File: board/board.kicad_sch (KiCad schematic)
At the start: 15 parts, among them J1 020_1000BASE-T_with_CT, J10 018_QSPI, J11 Conn_01x03_Male, J2 003_power, J3 008_USB, J4 001_I2C, J5 008_USB, J6 002_SPI, J7 010_UART, J8 015_RGMII, J9 010_UART, U2 TLV71318PQDBVRQ1

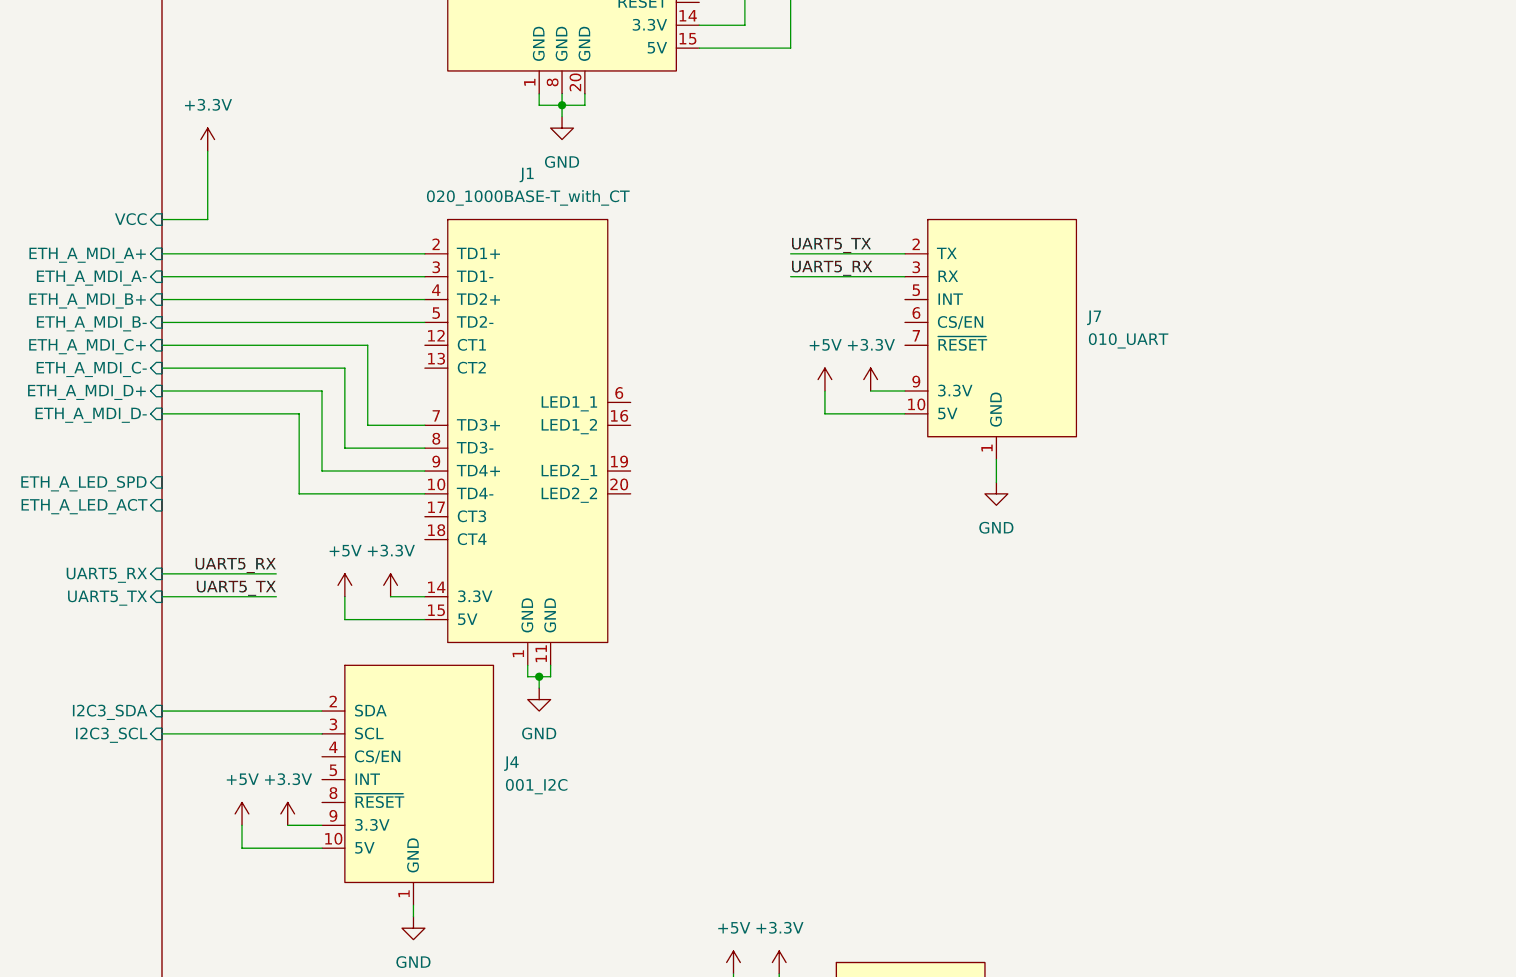
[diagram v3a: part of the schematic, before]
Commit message: increased spacing
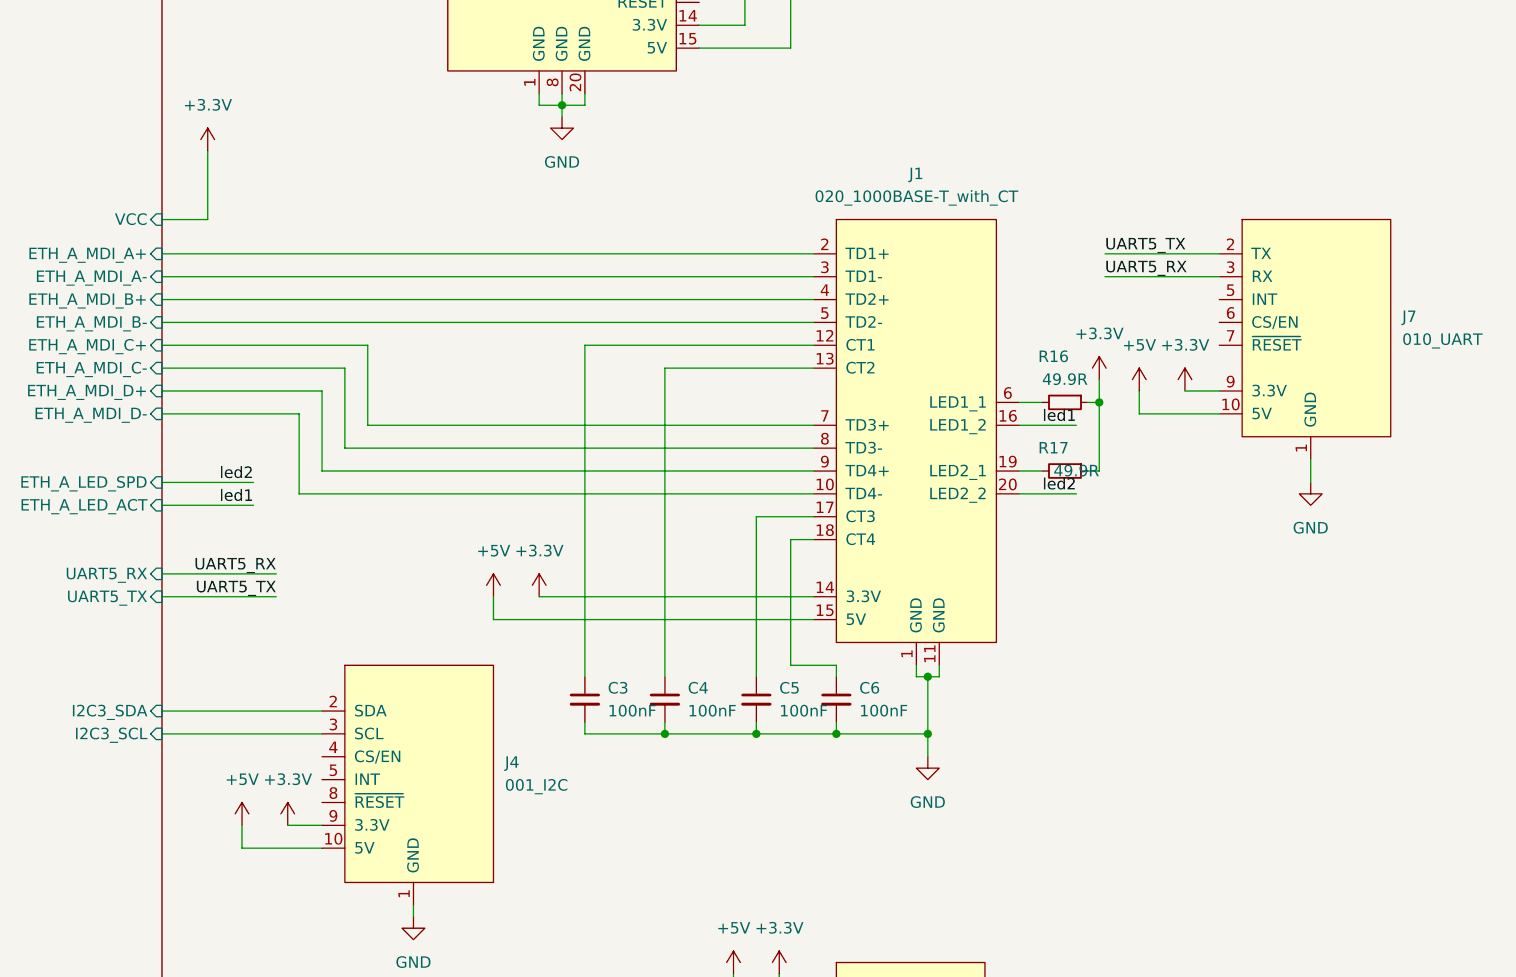
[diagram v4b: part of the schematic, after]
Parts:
- added C3, C4, C5, C6: 100nF, Capacitor_SMD:C_0603_1608Metric, symbol Device:C_Small
- added R16, R17: 49.9R, Resistor_SMD:R_0603_1608Metric, symbol Device:R_Small
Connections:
- net +3.3V: now also R16.1, R17.1
- net GND: now also C3.2, C4.2, C5.2, C6.2
- net at J1.12 (CT1): now also C3.1
- net at J1.13 (CT2): now also C4.1
- net led1: now reaches J1.16 (LED1_2)
- net at J1.17 (CT3): now also C5.1
- net at J1.18 (CT4): now also C6.1
- net at J1.19 (LED2_1): now also R17.2
- net led2: now reaches J1.20 (LED2_2)
- net at J1.6 (LED1_1): now also R16.2
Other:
- moved on the sheet: J1, J7

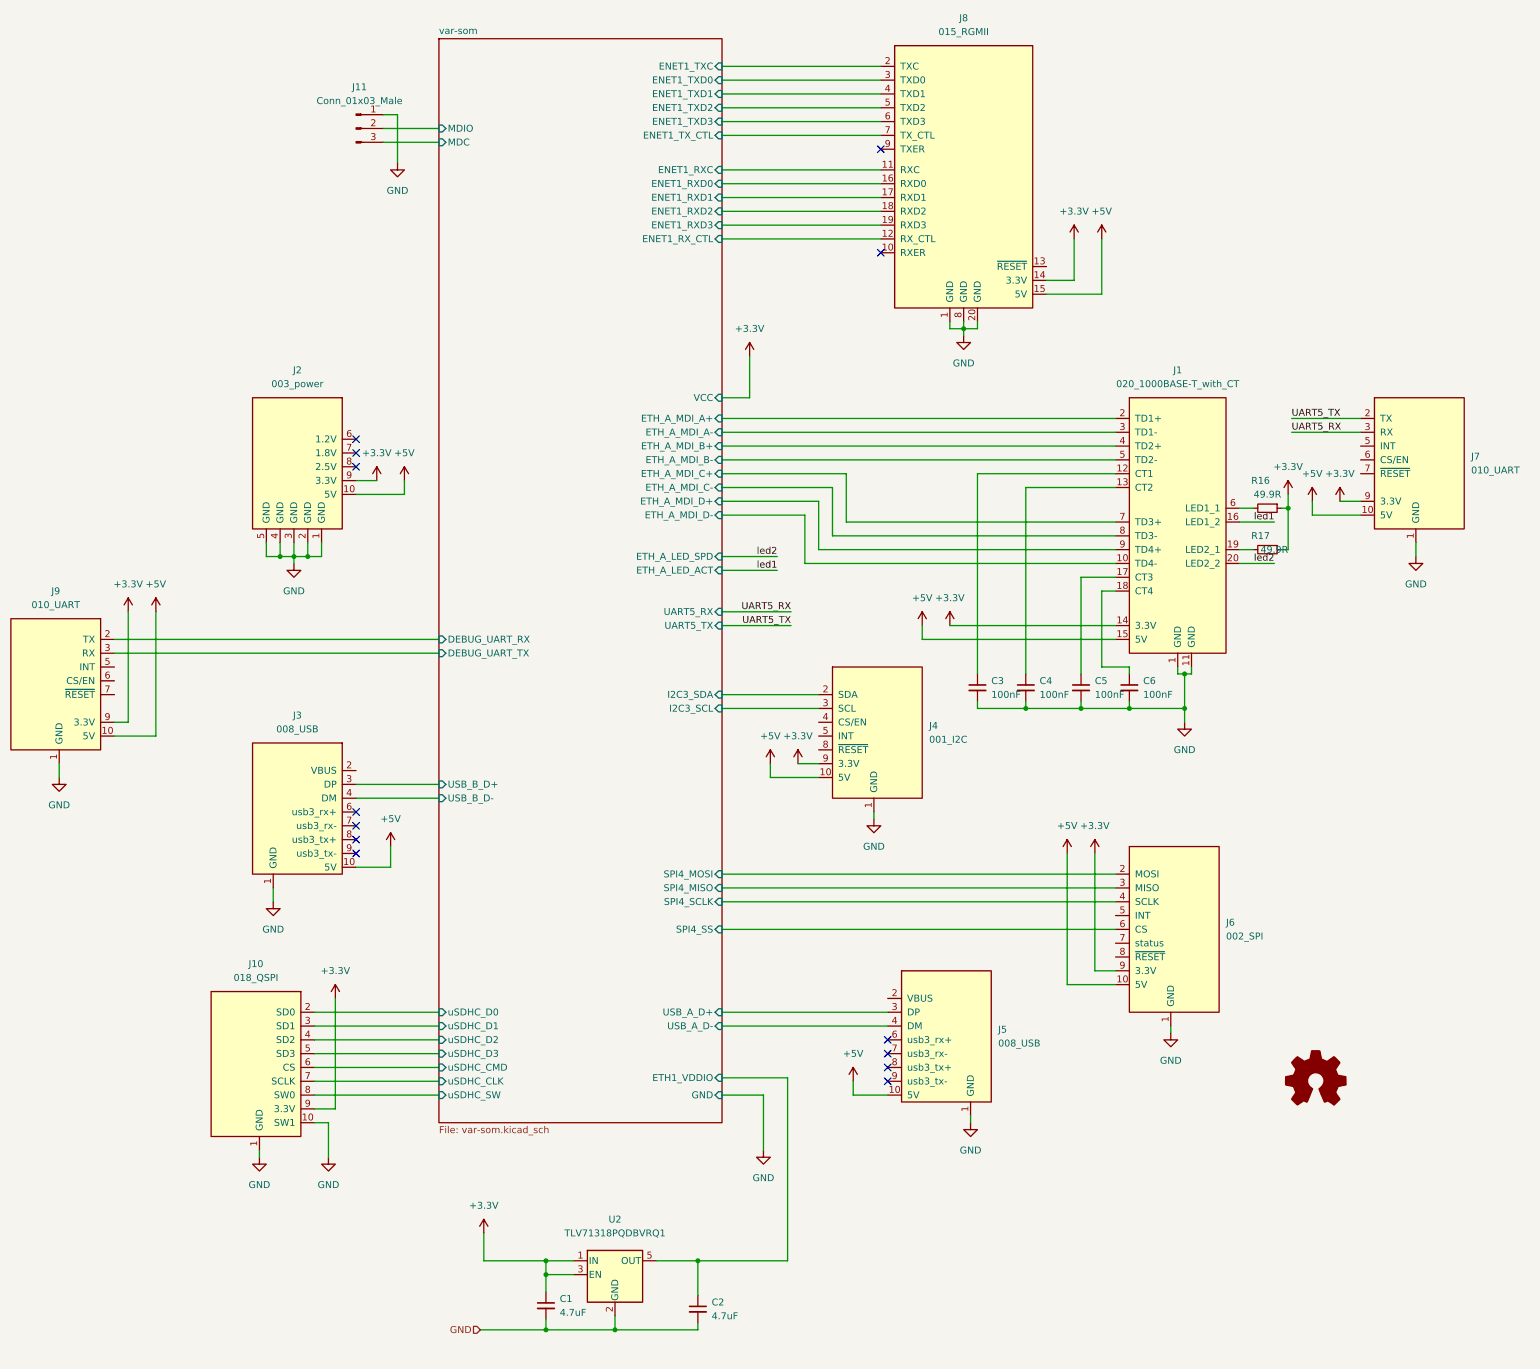
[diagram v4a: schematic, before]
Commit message: Update PU/PDn and values
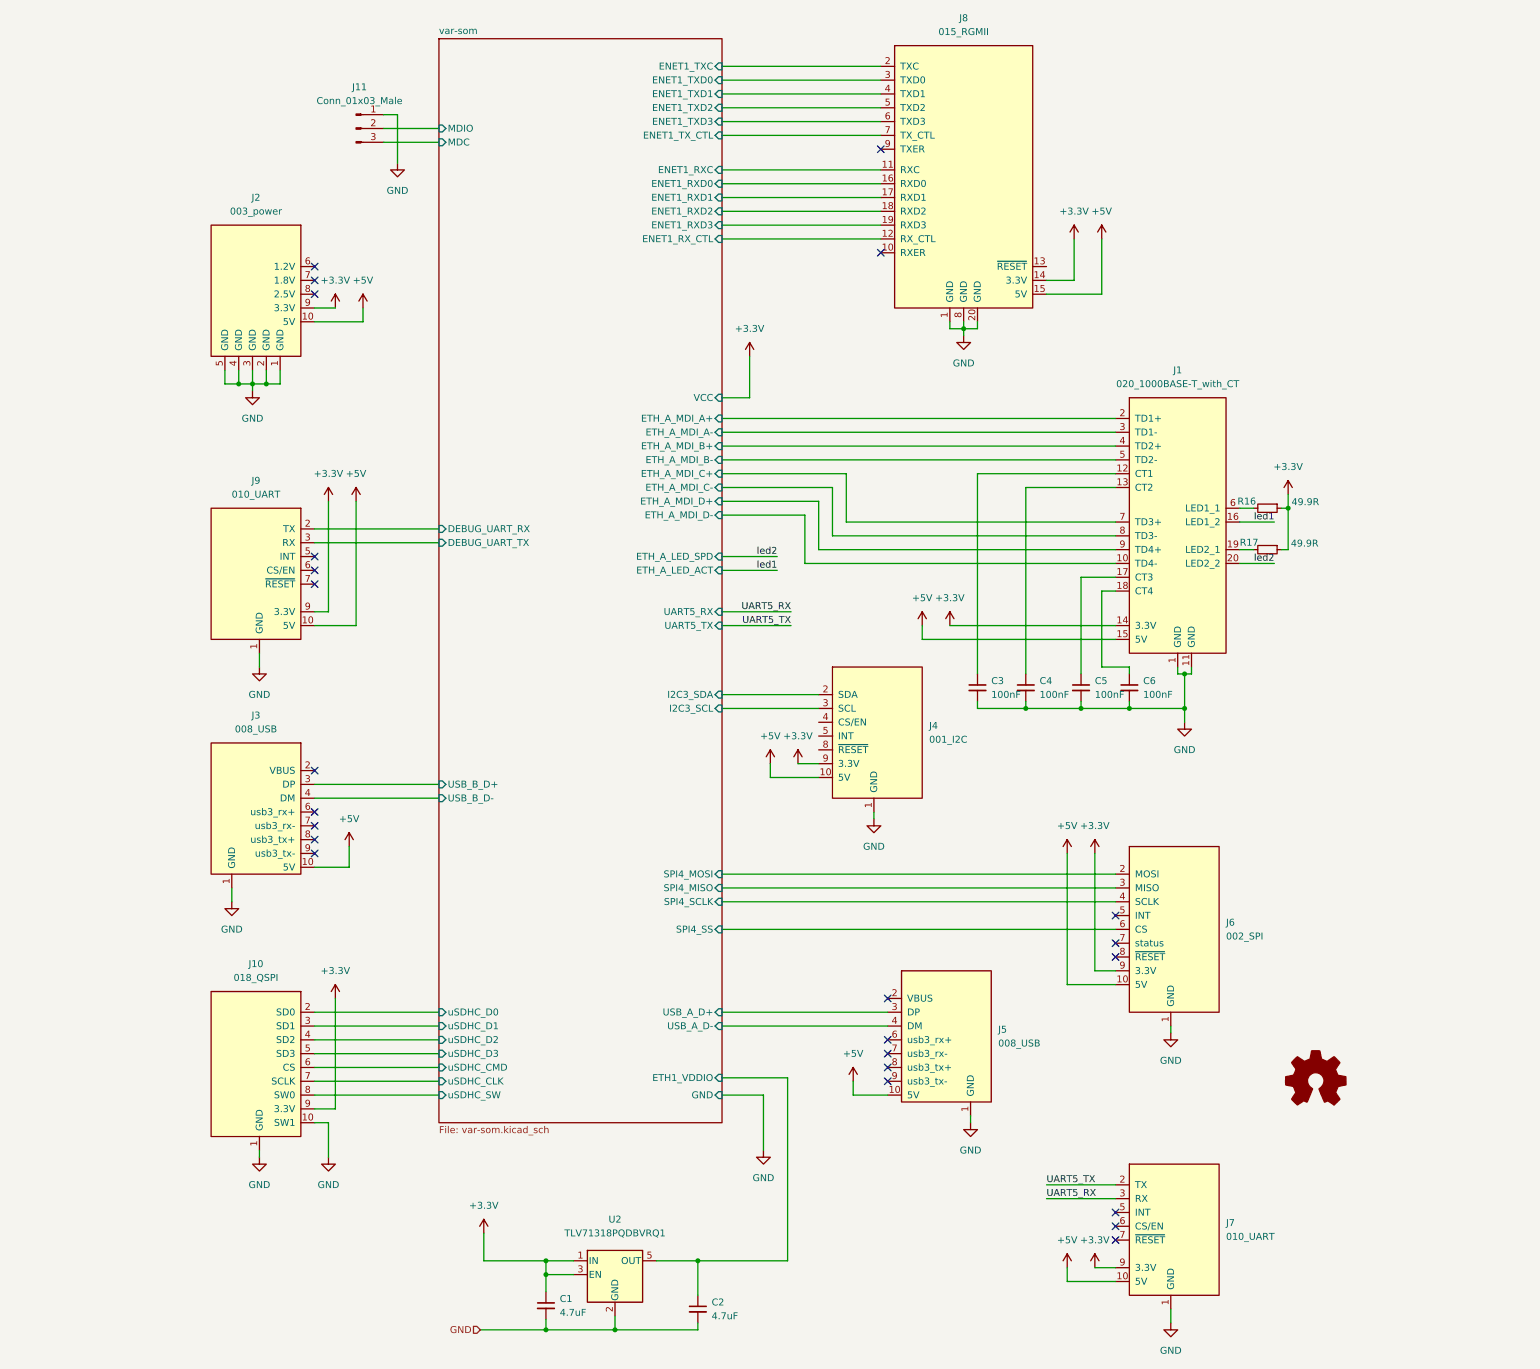
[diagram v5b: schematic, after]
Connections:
- no-connect marks 13 -> 24
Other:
- moved on the sheet: J2, J3, J7, J9
